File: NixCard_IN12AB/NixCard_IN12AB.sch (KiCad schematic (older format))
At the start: 8 parts, among them P1 CONN_01X06, P2 CONN_01X06, P3 TSW-104-07-F-S, P4 TSW-104-07-F-S, U1 HV513WG, U2 HV513WG

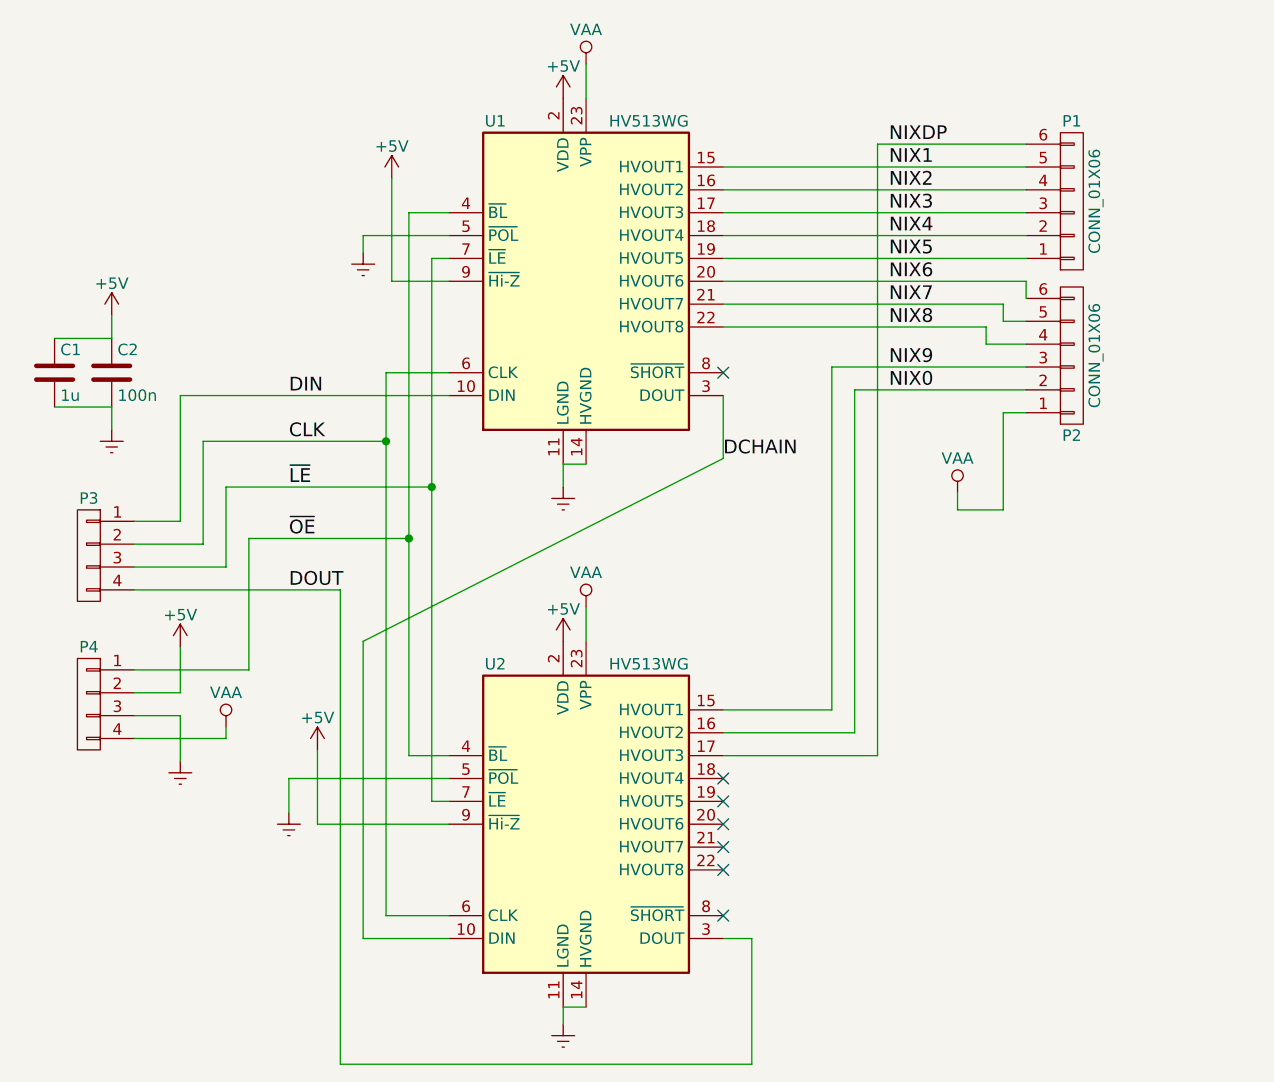
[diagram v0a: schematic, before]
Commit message: Corrects names (driver <-> IN12AB)
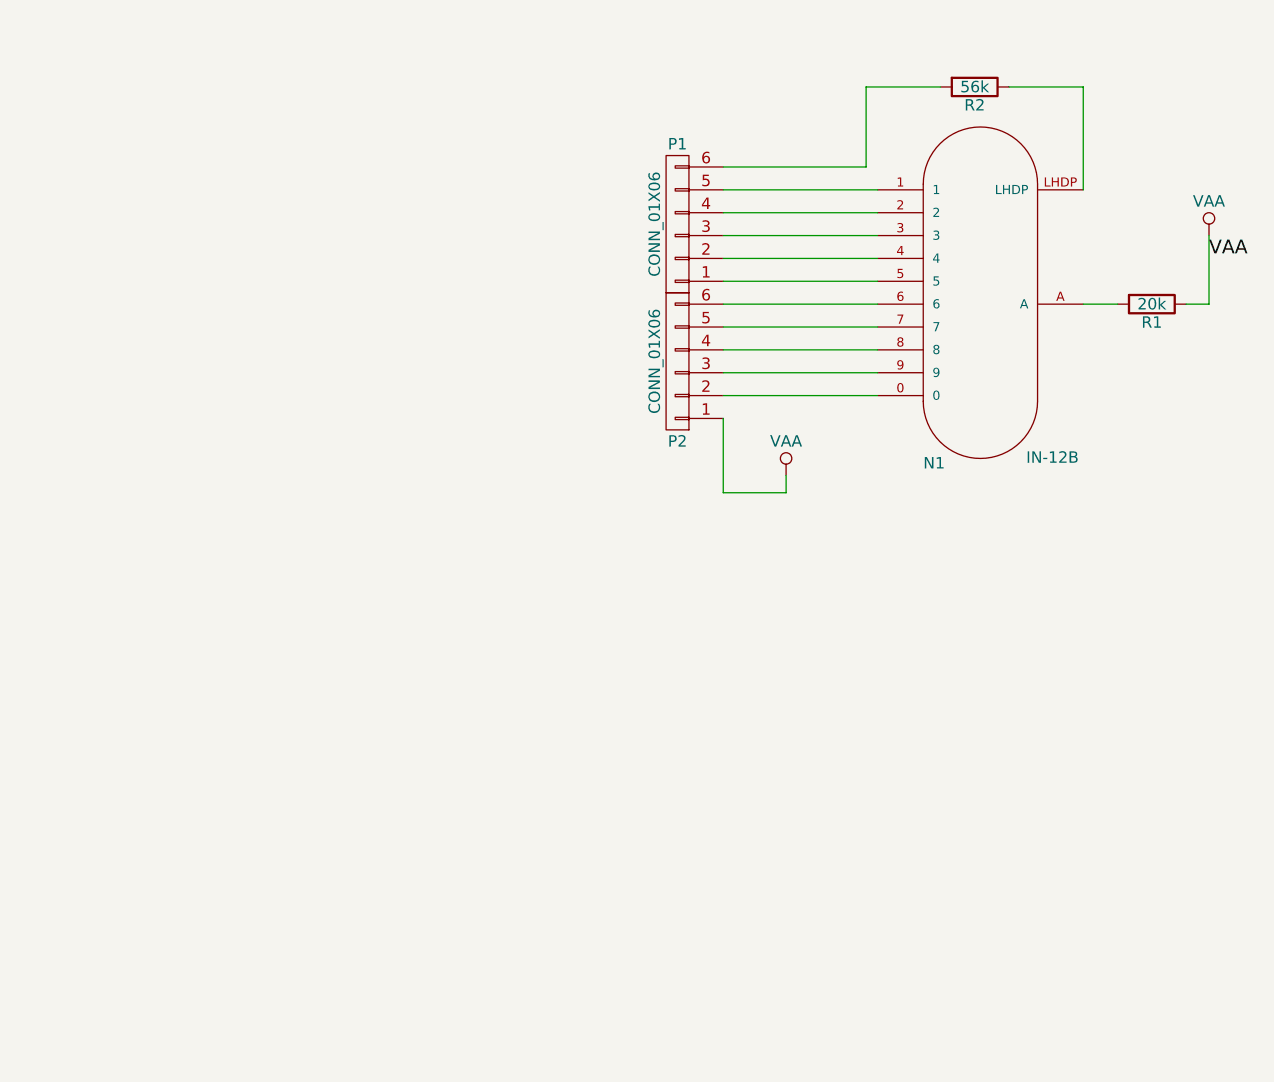
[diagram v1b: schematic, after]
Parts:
- removed C1: 1u, Capacitors_SMD:C_0603, symbol 1u
- removed C2: 100n, Capacitors_SMD:C_0603, symbol 100n
- removed P3, P4: TSW-104-07-F-S, Pin_Headers:Pin_Header_Straight_1x04_Pitch2.54mm, symbol TSW-104-07-F-S
- removed U1, U2: HV513WG, Package_SOIC:SOIC-24W_7.5x15.4mm_P1.27mm, symbol HV513WG
- added N1: IN-12B, footprints:IN-12B-skt, symbol IN-12B
- added R1: 20k, Resistors_SMD:R_0603, symbol 6k2
- added R2: 56k, Resistors_SMD:R_0603, symbol 6k2
- P1, P2: footprint Pin_Headers:Pin_Header_Straight_1x06_Pitch2.54mm -> Connectors_Samtec:SL-106-X-XX_1x06
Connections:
- net VAA: now also R1.1
- net NIX0: no longer names the net of P2.2 (P2)
- net NIX0: now also N1.0
- net NIX1: no longer names the net of P1.5 (P5)
- net NIX1: now also N1.1
- net NIX2: no longer names the net of P1.4 (P4)
- net NIX2: now also N1.2
- net NIX3: no longer names the net of P1.3 (P3)
- net NIX3: now also N1.3
- net NIX4: no longer names the net of P1.2 (P2)
- net NIX4: now also N1.4
- net NIX5: no longer names the net of P1.1 (P1)
- net NIX5: now also N1.5
- net NIX6: no longer names the net of P2.6 (P6)
- net NIX6: now also N1.6
- net NIX7: no longer names the net of P2.5 (P5)
- net NIX7: now also N1.7
- net NIX8: no longer names the net of P2.4 (P4)
- net NIX8: now also N1.8
- net NIX9: no longer names the net of P2.3 (P3)
- net NIX9: now also N1.9
- net NIXDP: no longer names the net of P1.6 (P6)
- net NIXDP: now also R2.2
- new net: N1.A, R1.2
- new net: N1.LHDP, R2.1
- no-connect marks 7 -> 0

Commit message: Initial IN-12AB board, gerbers
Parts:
- removed P1, P2: CONN_01X06, Connectors_Samtec:SL-106-X-XX_1x06, symbol CONN_01X06
- added P4, P5, P6, P7: CONN_01X05, Pin_Headers:Pin_Header_Straight_1x05_Pitch2.54mm, symbol CONN_01X05
- added R10, R11, R3, R4, R5, R6, R7, R8, R9: 20k, Resistors_SMD:R_0603, symbol 6k2
- R1: renamed from R2; value 56k -> 120k
- renumbered R1 to R2
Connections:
- net VAA: now also N1.A, P4.5 (P5), P5.1 (P1); no longer R2.1
- net HV1: now reaches R2.2
- net HV1: now also P5.3 (P3); no longer N1.A
- net at N1.0: now also R11.1
- net at N1.1: now also R2.1
- net at N1.2: now also R3.1
- net at N1.3: now also R4.1
- net at N1.4: now also R5.1
- net at N1.5: now also R6.1
- net at N1.6: now also R7.1
- net at N1.7: now also R8.1
- net at N1.8: now also R9.1
- net at N1.9: now also R10.1
- net HV10: now reaches R1.2
- net HV10: now also P7.2 (P2)
- new net GNDREF: P6.1 (P1), P7.5 (P5)
- new net HV0: P5.2 (P2), R11.2
- new net HV11: P7.1 (P1)
- new net HV12: P6.5 (P5)
- new net HV13: P6.4 (P4)
- new net HV14: P6.3 (P3)
- new net HV15: P6.2 (P2)
- new net HV2: P5.4 (P4), R3.2
- new net HV3: P5.5 (P5), R4.2
- new net HV4: P4.1 (P1), R5.2
- new net HV5: P4.2 (P2), R6.2
- new net HV6: P4.3 (P3), R7.2
- new net HV7: P4.4 (P4), R8.2
- new net HV8: P7.4 (P4), R9.2
- new net HV9: P7.3 (P3), R10.2
- no-connect marks 0 -> 5
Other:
- moved on the sheet: R2
